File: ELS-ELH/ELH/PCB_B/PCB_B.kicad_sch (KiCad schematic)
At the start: 20 parts, among them J11 Conn_01x09_Socket

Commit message: PCB B Advanced
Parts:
- added Bornera1: 5V Reg Output, ELH_Library:Bornera 2P, symbol Connector:Screw_Terminal_01x02
- added J1: Pressure Transducer Input, TerminalBlock:TerminalBlock_MaiXu_MX126-5.0-03P_1x03_P5.00mm, symbol Connector:Screw_Terminal_01x03
- added J3, J4: Conn_01x20_Pin, Connector_PinSocket_2.54mm:PinSocket_1x20_P2.54mm_Vertical, symbol Connector:Conn_01x20_Pin
- Bornera7: value COM Camera Screw Terminal -> UART BUS 2
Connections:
- net +5VA: no longer ADC1.10 (VDD), Adapter1.1 (VCC), C13.1, C2.2, Converter1.1 (VB), ESP1.15 (VIN)
- net GND: now also Adapter1.2 (GND), BME2.3 (GND), BZ1.2 (-), C13.2, C2.1, D10.2 (K), ESP1.14 (GND), ESP1.17 (GND), IMU3.3 (GND), J11.8 (Pin_8), SD_Adapter1.6 (GND), W25QXX1.4 (GND), Bornera1.1 (Pin_1), J1.2 (Pin_2)
- net GND1: no longer Adapter1.2 (GND), BME2.3 (GND), BZ1.2 (-), C13.2, C2.1, D10.2 (K), ESP1.14 (GND), IMU3.3 (GND), J11.8 (Pin_8), SD_Adapter1.6 (GND), W25QXX1.4 (GND)
- new net +5V: ADC1.10 (VDD), Adapter1.1 (VCC), Bornera1.2 (Pin_2), C13.1, C2.2, Converter1.1 (VB), ESP1.15 (VIN), J1.3 (Pin_3)
- new net PT_ADC1: J1.1 (Pin_1)
- no-connect marks 37 -> 36

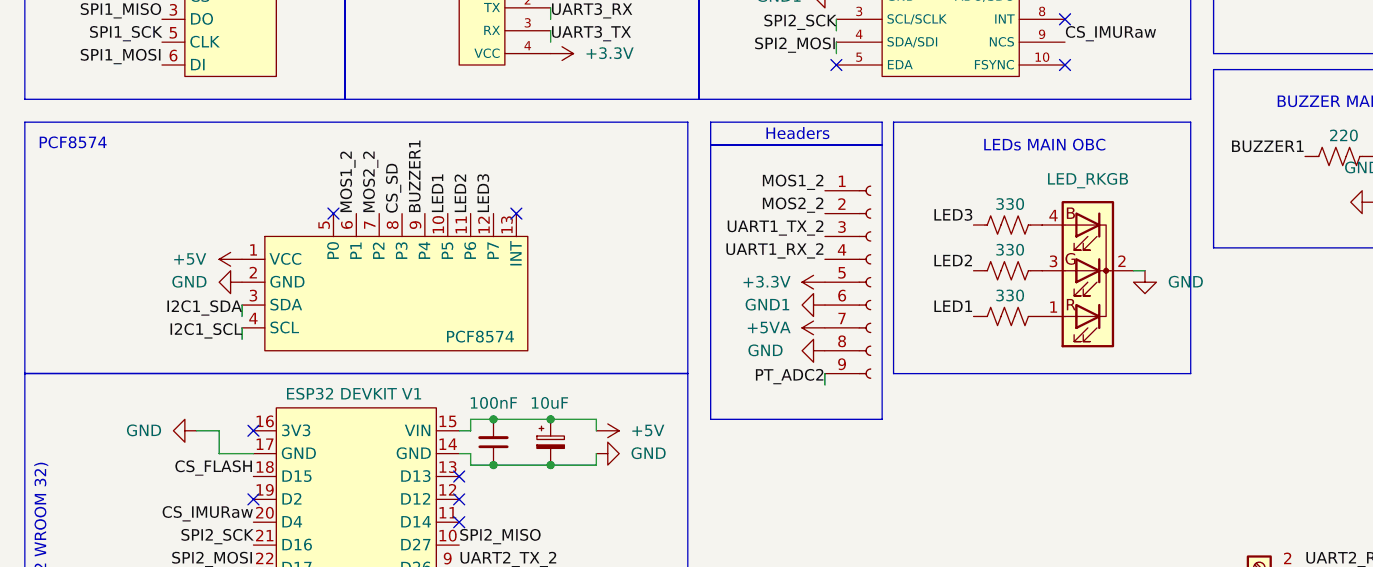
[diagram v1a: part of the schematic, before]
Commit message: Updates
The boost component was replaced, capacitors were added for the regulator, and the power supply voltage for the expansion module was changed
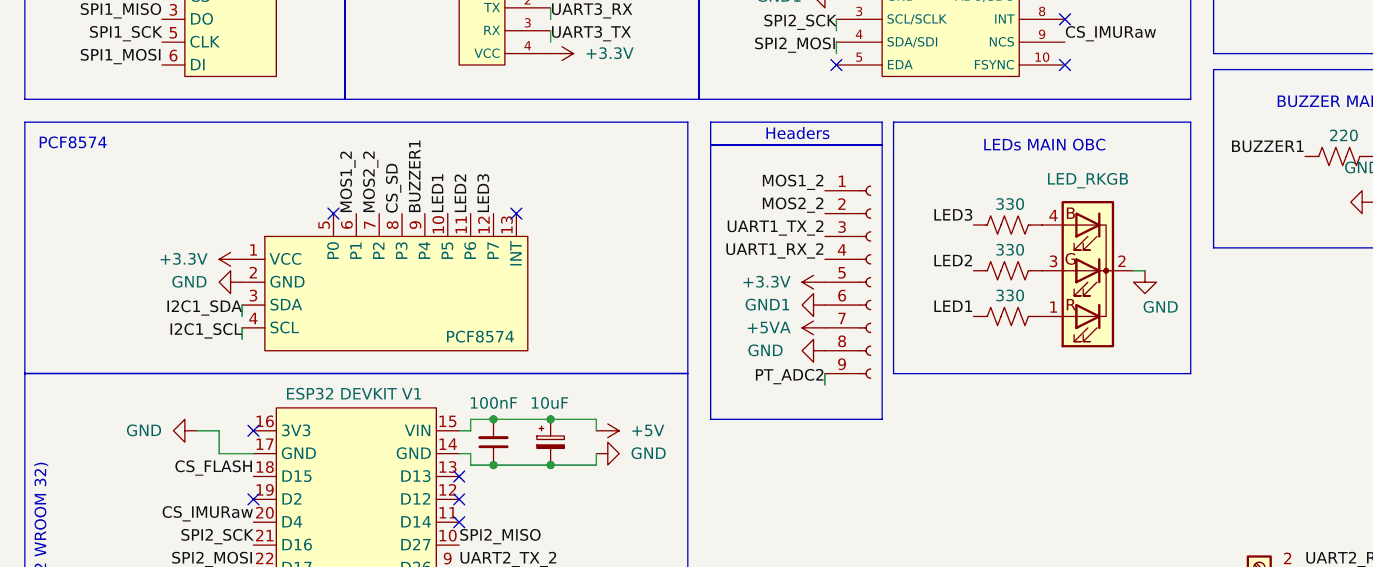
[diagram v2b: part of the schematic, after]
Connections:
- net +3.3V: now also Adapter1.1 (VCC)
- net +5V: no longer Adapter1.1 (VCC)
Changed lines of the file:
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@@
 	)
 	(symbol
+		(lib_id "power:+3.3V")
+		(at 48.26 86.36 90)
+		(unit 1)
+		(exclude_from_sim no)
+		(in_bom yes)
+		(on_board yes)
+		(dnp no)
+		(fields_autoplaced yes)
+		(property "Reference" "#PWR09"
+			(at 52.07 86.36 0)
+			(effects
+				(font
+					(size 1.27 1.27)
+				)
+				(hide yes)
+			)
+		)
+		(property "Value" "+3.3V"
+			(at 44.45 86.3599 90)
+			(effects
+				(font
+					(size 1.27 1.27)
+				)
+				(justify left)
+			)
+		)
+		(property "Footprint" ""
+			(at 48.26 86.36 0)
+			(effects
+				(font
+					(size 1.27 1.27)
+				)
+				(hide yes)
+			)
+		)
+		(property "Datasheet" ""
+			(at 48.26 86.36 0)
+			(effects
+				(font
+					(size 1.27 1.27)
+				)
+				(hide yes)
+			)
+		)
+		(property "Description" "Power symbol creates a global label with name \"+3.3V\""
+			(at 48.26 86.36 0)
+			(effects
+				(font
+					(size 1.27 1.27)
+				)
+				(hide yes)
+			)
+		)
+		(pin "1"
+		)
+		(instances
+			(project "PCB_B"
+				(path "/8ce3d015-2fa7-4d89-b6ca-9a5bdbe9d762"
+					(reference "#PWR09")
+					(unit 1)
+				)
+			)
+		)
+	)
+	(symbol
 		(lib_id "power:GND1")
 		(at 166.37 132.08 90)
@@
 	)
 	(symbol
-		(lib_id "power:+5VA")
-		(at 48.26 86.36 90)
-		(unit 1)
-		(exclude_from_sim no)
-		(in_bom yes)
-		(on_board yes)
-		(dnp no)
-		(property "Reference" "#PWR052"
-			(at 52.07 86.36 0)
-			(effects
-				(font
-					(size 1.27 1.27)
-				)
-				(hide yes)
-			)
-		)
-		(property "Value" "+5V"
-			(at 42.418 86.36 90)
-			(effects
-				(font
-					(size 1.27 1.27)
-				)
-			)
-		)
-		(property "Footprint" ""
-			(at 48.26 86.36 0)
-			(effects
-				(font
-					(size 1.27 1.27)
-				)
-				(hide yes)
-			)
-		)
-		(property "Datasheet" ""
-			(at 48.26 86.36 0)
-			(effects
-				(font
-					(size 1.27 1.27)
-				)
-				(hide yes)
-			)
-		)
-		(property "Description" "Power symbol creates a global label with name \"+5VA\""
-			(at 48.26 86.36 0)
-			(effects
-				(font
-					(size 1.27 1.27)
-				)
-				(hide yes)
-			)
-		)
-		(pin "1"
-		)
-		(instances
-			(project "PCB_B"
-				(path "/8ce3d015-2fa7-4d89-b6ca-9a5bdbe9d762"
-					(reference "#PWR052")
-					(unit 1)
-				)
-			)
-		)
-	)
-	(symbol
 		(lib_id "power:+3.3V")
 		(at 71.12 31.75 90)
@@
 		(on_board yes)
 		(dnp no)
-		(fields_autoplaced yes)
 		(property "Reference" "#PWR04"
 			(at 148.59 93.98 0)
@@
 		)
 		(property "Value" "GND"
-			(at 151.13 88.8999 0)
+			(at 148.336 91.694 0)
 			(effects
 				(font
